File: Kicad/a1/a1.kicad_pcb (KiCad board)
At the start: 2 copper layers, 190 x 100 mm, 126 parts, among them J1 Conn_02x03_Odd_Even, J2 VGA, J3 AudioJack4, J4 Conn_02x17_Odd_Even, J6 Barrel Jack, J7 DE9_Plug, J8 DE9_Plug, SW1 Q, SW10 P, SW11 A, SW12 S, SW13 D, SW14 F, SW15 G, SW16 H, SW17 J, SW18 K, SW19 L, SW2 W, SW20 ENT, SW21 SHIFT, SW22 Z, SW23 X, SW24 C, SW25 V, SW26 B, SW27 N, SW28 M, SW29 SPACE, SW3 E, SW30 ALT, SW31 SW_Push, SW32 SW_SPDT, SW4 R, SW5 T, SW6 Y, SW7 U, SW8 I, SW9 O, U1 74HC590A, U10 74HC32, U11 74HC174, U12 74HC4520, U2 74HC590A, U3 62256, U4 SST39SF0x0, U5 W65C02SxP, U6 74HCT540, U7 74HC166, U8 74HC14, U9 74HC10, Y1 16Mhz

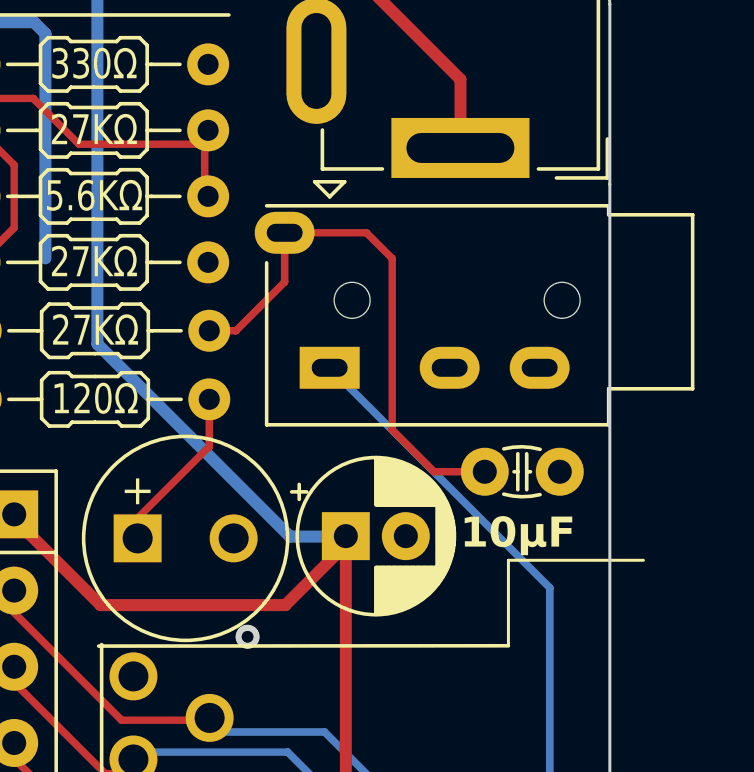
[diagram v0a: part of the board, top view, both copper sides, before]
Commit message: fix PJ-320A (headphone jack) footprint
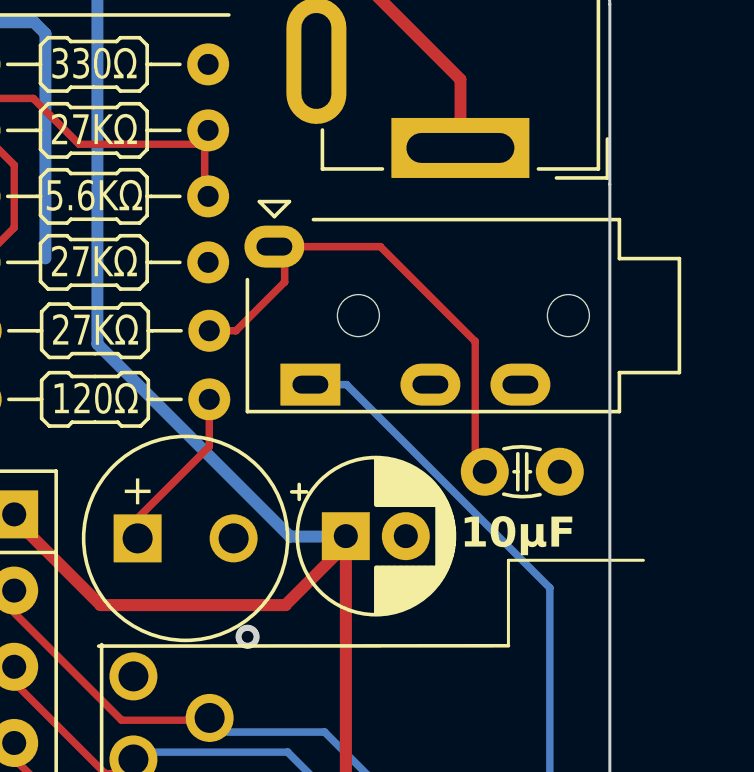
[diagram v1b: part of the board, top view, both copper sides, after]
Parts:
- moved J3 3.82 mm to (214.2, 51.7)
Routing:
- net /DataOut: track 18.1 -> 16.5 mm
- net /AUDIN: track 166.3 -> 167.0 mm
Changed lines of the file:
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@@
 	(footprint "Smal:Jack_3.5mm_PJ320A_Horizontal"
 		(layer "F.Cu")
-		(at 216.891 48.929 -90)
+		(at 214.249 51.689 -90)
 		(descr "Headphones with microphone connector, 3.5mm, 4 pins (http://www.qingpu-electronics.com/en/products/WQP-PJ320E-177.html)")
 		(tags "3.5mm jack mic microphone phones headphones 4pins audio plug")
 		(property "Reference" "J3"
-			(at 2.54 -13.97 90)
+			(at -0.21 -15.97 90)
 			(layer "F.SilkS")
 			(hide yes)
@@
 		)
 		(property "Value" "AudioJack4"
-			(at 2.08 5.715 180)
+			(at -0.67 3.715 180)
 			(layer "F.Fab")
+			(hide yes)
 			(effects
 				(font
@@
 		)
 		(property "Footprint" "Smal:Jack_3.5mm_PJ320A_Horizontal"
-			(at 0 0 -90)
+			(at -2.75 -2 -90)
 			(unlocked yes)
 			(layer "F.Fab")
@@
 		)
 		(property "Datasheet" ""
-			(at 0 0 -90)
+			(at -2.75 -2 -90)
 			(unlocked yes)
 			(layer "F.Fab")
@@
 		)
 		(property "Description" "Audio Jack, 4 Poles (TRRS)"
-			(at 0 0 -90)
+			(at -2.75 -2 -90)
 			(unlocked yes)
 			(layer "F.Fab")
@@
 		(attr through_hole)
 		(fp_line
-			(start 6.4 2.1)
-			(end 1 2.1)
+			(start 3.2 0.1)
+			(end -1.2 0.1)
 			(stroke
 				(width 0.12)
@@
 		)
 		(fp_line
-			(start -1.7 0.5)
-			(end -1.2 0)
+			(start -3.8 -0.3)
+			(end -3.3 -0.8)
 			(stroke
 				(width 0.12)
@@
 		)
 		(fp_line
-			(start -1.2 0)
-			(end -1.7 -0.5)
+			(start -3.3 -0.8)
+			(end -3.8 -1.3)
 			(stroke
 				(width 0.12)
@@
 		)
 		(fp_line
-			(start -1.7 -0.5)
-			(end -1.7 0.5)
+			(start -3.8 -1.3)
+			(end -3.8 -0.3)
 			(stroke
 				(width 0.12)
@@
 		)
 		(fp_line
-			(start -0.9 -9.3)
-			(end -0.9 2.1)
+			(start -3.2 -12.3)
+			(end -3.2 -2.1)
 			(stroke
 				(width 0.12)
@@
 		)
 		(fp_line
-			(start -0.9 -9.3)
-			(end -0.6 -9.3)
+			(start -3.2 -12.3)
+			(end -1.9 -12.3)
 			(stroke
 				(width 0.12)
@@
 		)
 		(fp_line
-			(start -0.6 -9.3)
-			(end -0.6 -12.1)
+			(start -1.9 -12.3)
+			(end -1.9 -14.3)
 			(stroke
 				(width 0.12)
@@
 		)
 		(fp_line
-			(start 5.2 -9.3)
-			(end 6.4 -9.3)
+			(start 1.9 -12.3)
+			(end 3.2 -12.3)
 			(stroke
 				(width 0.12)
@@
 		)
 		(fp_line
-			(start 5.2 -9.3)
-			(end 5.2 -12.1)
+			(start 1.9 -12.3)
+			(end 1.9 -14.3)
 			(stroke
 				(width 0.12)
@@
 		)
 		(fp_line
-			(start 6.4 -9.3)
-			(end 6.4 2.1)
+			(start 3.2 -12.3)
+			(end 3.2 0.1)
 			(stroke
 				(width 0.12)
@@
 		)
 		(fp_line
-			(start 5.2 -12.1)
-			(end -0.6 -12.1)
+			(start 1.9 -14.3)
+			(end -1.9 -14.3)
 			(stroke
 				(width 0.12)
@@
 		)
 		(fp_line
-			(start -1.3 3)
-			(end 6.8 3)
+			(start -4.05 0)
+			(end 4.05 0)
 			(stroke
 				(width 0.05)
@@
 		)
 		(fp_line
-			(start -1.3 -12.5)
-			(end -1.3 3)
+			(start -4.05 -15.5)
+			(end -4.05 0)
 			(stroke
 				(width 0.05)
@@
 		)
 		(fp_line
-			(start -1.3 -12.5)
-			(end 6.8 -12.5)
+			(start -4.05 -15.5)
+			(end 4.05 -15.5)
 			(stroke
 				(width 0.05)
@@
 		)
 		(fp_line
-			(start 6.8 -12.5)
-			(end 6.8 3)
+			(start 4.05 -15.5)
+			(end 4.05 0)
 			(stroke
 				(width 0.05)
@@
 		)
 		(fp_line
-			(start -0.8 2)
-			(end -0.8 -9.2)
-			(stroke
-				(width 0.1)
-				(type solid)
-			)
-			(layer "F.Fab")
-		)
-		(fp_line
-			(start 3.7 2)
-			(end -0.8 2)
-			(stroke
-				(width 0.1)
-				(type solid)
-			)
-			(layer "F.Fab")
-		)
-		(fp_line
-			(start 6.3 2)
-			(end 5.3 2)
-			(stroke
-				(width 0.1)
-				(type solid)
-			)
-			(layer "F.Fab")
-		)
-		(fp_line
-			(start -0.8 -9.2)
-			(end -0.5 -9.2)
-			(stroke
-				(width 0.1)
-				(type solid)
-			)
-			(layer "F.Fab")
-		)
-		(fp_line
-			(start -0.5 -9.2)
-			(end -0.5 -12)
-			(stroke
-				(width 0.1)
-				(type solid)
-			)
-			(layer "F.Fab")
-		)
-		(fp_line
-			(start 5.1 -9.2)
-			(end 6.3 -9.2)
+			(start -2.3 0)
+			(end -2.3 -12.2)
 			(stroke
 				(width 0.1)
-				(type solid)
+				(type default)
 			)
 			(layer "F.Fab")
 		)
 		(fp_line
-			(start 6.3 -9.2)
-			(end 6.3 2)
+			(start 2.3 0)
+			(end 2.3 -12.2)
 			(stroke
 				(width 0.1)
-				(type solid)
+				(type default)
 			)
 			(layer "F.Fab")
 		)
-		(fp_line
-			(start -0.5 -12)
-			(end 5.1 -12)
+		(fp_rect
+			(start -3.1 -12.2)
+			(end 3.1 0)
 			(stroke
 				(width 0.1)
-				(type solid)
+				(type default)
 			)
+			(fill none)
 			(layer "F.Fab")
 		)
-		(fp_line
-			(start 5.1 -12)
-			(end 5.1 -9.2)
+		(fp_rect
+			(start -1.8 -14.2)
+			(end 1.8 -12.2)
 			(stroke
 				(width 0.1)
-				(type solid)
-			)
-			(layer "F.Fab")
-		)
-		(fp_circle
-			(center 0.9 0)
-			(end 1.2 0.15)
-			(stroke
-				(width 0.12)
-				(type solid)
+				(type default)
 			)
 			(fill none)
@@
 		)
 		(fp_text user "${REFERENCE}"
-			(at 2.54 -13.97 90)
+			(at 0 1.1 90)
 			(layer "F.Fab")
 			(effects
@@
 		)
 		(pad "" np_thru_hole circle
-			(at 2.25 -7.75 180)
-			(size 1.2 1.2)
-			(drill 1.2)
-			(layers "*.Cu" "*.Mask")
+			(at 0 -10.6 180)
+			(size 1 1)
+			(drill 1.4)
+			(layers "F&B.Cu" "*.Mask")
 		)
 		(pad "" np_thru_hole circle
-			(at 2.25 -0.75 180)
+			(at 0 -3.6 180)
 			(size 1.2 1.2)
-			(drill 1.2)
-			(layers "*.Cu" "*.Mask")
+			(drill 1.4)
+			(layers "F&B.Cu" "*.Mask")
 		)
 		(pad "R1" thru_hole oval
-			(at 4.5 -4 180)
+			(at 2.3 -6 180)
 			(size 2 1.4)
 			(drill oval 1.2 0.6)
@@
 		)
 		(pad "R2" thru_hole oval
-			(at 4.5 -7 180)
+			(at 2.3 -9 180)
 			(size 2 1.4)
 			(drill oval 1.2 0.6)
@@
 		)
 		(pad "S" thru_hole oval
-			(at 0 1.5 180)
+			(at -2.3 -0.8 180)
 			(size 2 1.4)
 			(drill oval 1.2 0.6)
@@
 		)
 		(pad "T" thru_hole rect
-			(at 4.5 0 180)
+			(at 2.3 -2 180)
 			(size 2 1.4)
 			(drill oval 1.2 0.6)
@@
 	)
 	(segment
+		(start 224.23 98.625427)
+		(end 224.23 60.765)
+		(width 0.25)
+		(layer "B.Cu")
+		(net 69)
+	)
+	(segment
 		(start 128.98 81.36)
 		(end 124.62 77)
@@
 	)
 	(segment
-		(start 224.23 60.765)
-		(end 217.055 53.59)
+		(start 128.98 95.325)
+		(end 128.98 81.36)
 		(width 0.25)
 		(layer "B.Cu")
@@
 	)
 	(segment
-		(start 224.23 98.625427)
-		(end 224.23 60.765)
+		(start 224.23 60.765)
+		(end 217.454 53.989)
 		(width 0.25)
 		(layer "B.Cu")
@@
 	)
 	(segment
-		(start 128.98 95.325)
-		(end 128.98 81.36)
+		(start 217.454 53.989)
+		(end 216.249 53.989)
 		(width 0.25)
 		(layer "B.Cu")
@@
 	)
 	(segment
-		(start 213.767 52.195)
-		(end 215.391 50.571)
+		(start 218.581 49.389)
+		(end 215.391 49.389)
 		(width 0.25)
 		(layer "F.Cu")
@@
 	)
 	(segment
-		(start 215.391 50.571)
-		(end 215.391 48.929)
+		(start 221.742 52.55)
+		(end 218.581 49.389)
 		(width 0.25)
 		(layer "F.Cu")
@@
 	)
 	(segment
-		(start 218.121 48.929)
-		(end 215.391 48.929)
+		(start 215.391 49.389)
+		(end 215.391 50.571)
 		(width 0.25)
 		(layer "F.Cu")
@@
 	)
 	(segment
-		(start 218.974 55.497)
-		(end 218.974 49.782)
+		(start 222.062 56.894)
+		(end 221.742 56.574)
 		(width 0.25)
 		(layer "F.Cu")
@@
 	)
 	(segment
-		(start 212.878 52.195)
+		(start 215.391 50.571)
 		(end 213.767 52.195)
 		(width 0.25)
@@
 	)
 	(segment
-		(start 220.371 56.894)
-		(end 218.974 55.497)
-		(width 0.25)
-		(layer "F.Cu")
-		(net 104)
-	)
-	(segment
-		(start 218.974 49.782)
-		(end 218.121 48.929)
+		(start 213.767 52.195)
+		(end 212.878 52.195)
 		(width 0.25)
 		(layer "F.Cu")
@@
 	)
 	(segment
-		(start 222.062 56.894)
-		(end 220.371 56.894)
+		(start 221.742 56.574)
+		(end 221.742 52.55)
 		(width 0.25)
 		(layer "F.Cu")
